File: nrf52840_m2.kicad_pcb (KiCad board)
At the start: 4 copper layers, 22 x 25.5 mm, 64 parts, among them J1 Bus_M.2_Socket_B, J2 Jlink-Tag connect, Q1 pmos, U1 nRF52840, U2 AP2112K-3.3, U3 MCP73831-2-OT, Y1 32.768kHz, Y2 32MHz

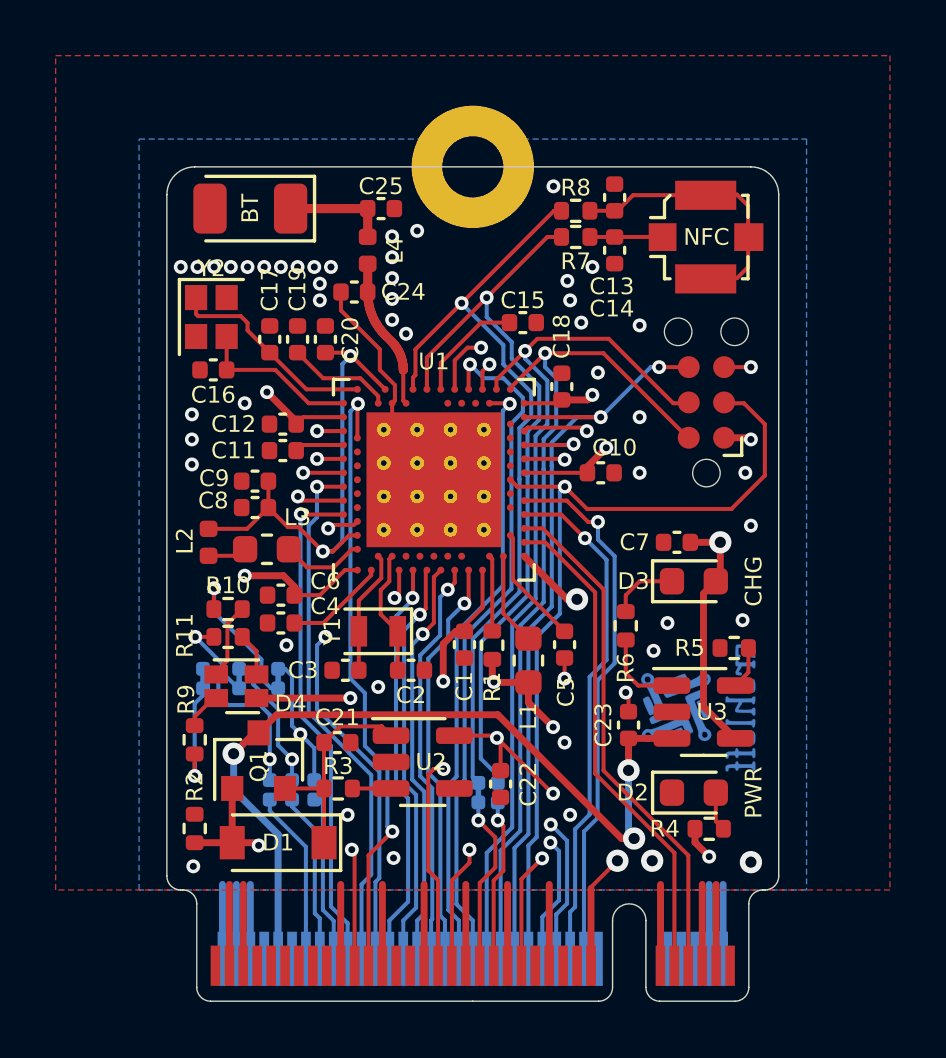
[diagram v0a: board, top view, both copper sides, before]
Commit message: update 3D/docs/fiducials
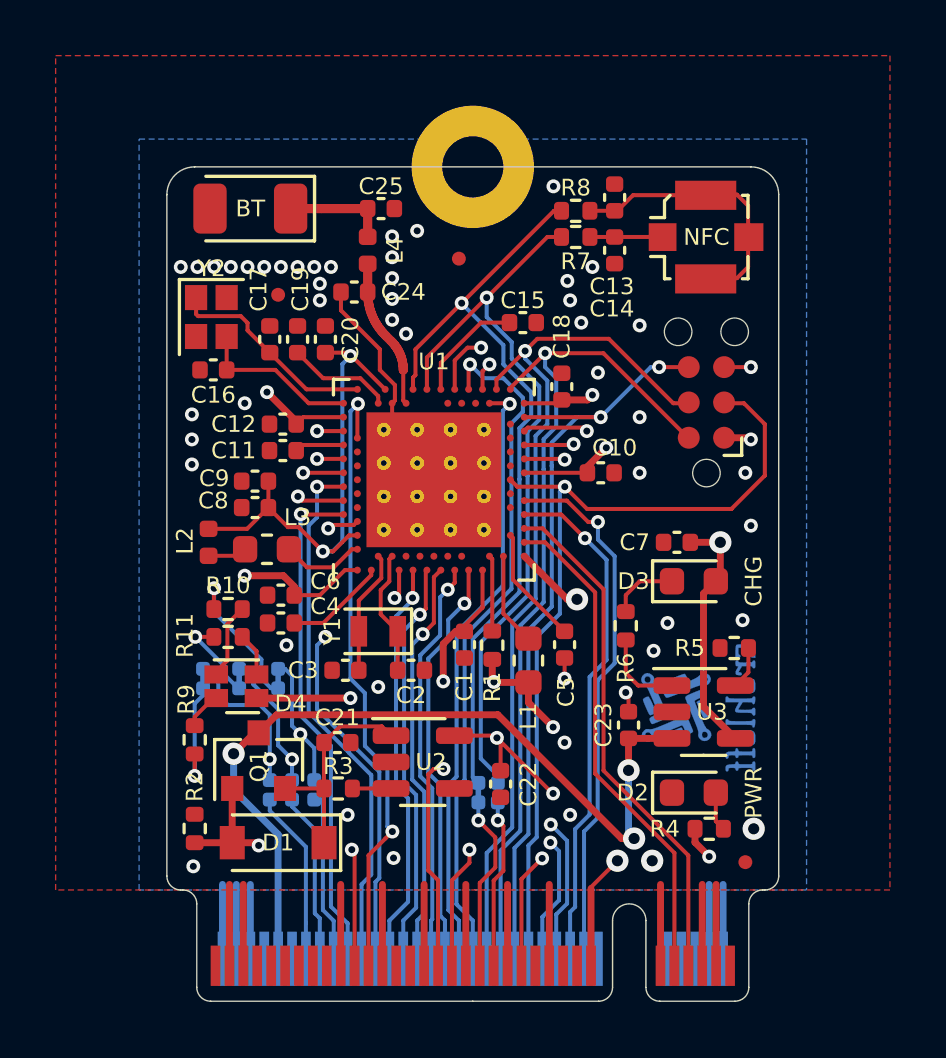
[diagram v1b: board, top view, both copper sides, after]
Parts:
- added FID1: Fiducial, Fiducial:Fiducial_0.5mm_Mask1mm, F.Cu at (228.8, 149.0)
- added FID2: Fiducial, Fiducial:Fiducial_0.5mm_Mask1mm, F.Cu at (212.0, 128.6)
- added FID3: Fiducial, Fiducial:Fiducial_0.5mm_Mask1mm, F.Cu at (218.5, 127.3)

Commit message: update files
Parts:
- moved FID1 0.51 mm to (229.2, 149.2)
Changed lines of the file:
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@@
       (effects (font (size 0.8 0.8) (thickness 0.12)))
     )
-    (pad 2 smd roundrect (at 1.45 0 180) (size 1.2 1.8) (layers F.Cu F.Paste F.Mask) (roundrect_rratio 0.208333)
+    (pad 2 smd roundrect (at 1.45 0 180) (size 1.2 1.8) (layers F.Cu F.Paste F.Mask) (roundrect_rratio 0.2083325)
       (net 23 "Net-(AE1-Pad2)"))
-    (pad 1 smd roundrect (at -1.45 0 180) (size 1.2 1.8) (layers F.Cu F.Paste F.Mask) (roundrect_rratio 0.208333)
+    (pad 1 smd roundrect (at -1.45 0 180) (size 1.2 1.8) (layers F.Cu F.Paste F.Mask) (roundrect_rratio 0.2083325)
       (net 22 "Net-(AE1-Pad1)"))
     (model ${KISYS3DMOD}/RF_Antenna.3dshapes/Johanson_2450AT18x100.wrl
@@
   )
   (module Fiducial:Fiducial_0.5mm_Mask1mm (layer F.Cu)
-    (at 228.8 149)
+    (at 229.25 149.25)
     (descr "Circular Fiducial, 0.5mm bare copper, 1mm soldermask opening (Level C)")
     (tags fiducial)
@@
       (effects (font (size 1 1) (thickness 0.15)))
     )
+    (fp_circle (center 0 0) (end 0.5 0) (layer F.Fab) (width 0.1))
+    (fp_circle (center 0 0) (end 0.75 0) (layer F.CrtYd) (width 0.05))
     (fp_text user %R (at 0 0) (layer F.Fab)
       (effects (font (size 0.2 0.2) (thickness 0.04)))
     )
-    (fp_circle (center 0 0) (end 0.5 0) (layer F.Fab) (width 0.1))
-    (fp_circle (center 0 0) (end 0.75 0) (layer F.CrtYd) (width 0.05))
     (pad "" smd circle (at 0 0) (size 0.5 0.5) (layers F.Cu F.Mask)
       (solder_mask_margin 0.25) (clearance 0.25))

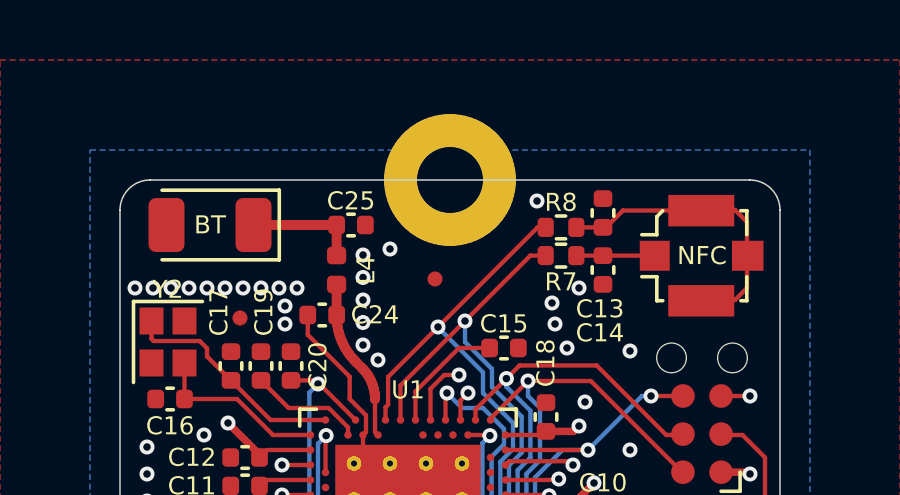
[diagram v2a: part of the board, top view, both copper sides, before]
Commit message: adjust m.2 mounting diameter
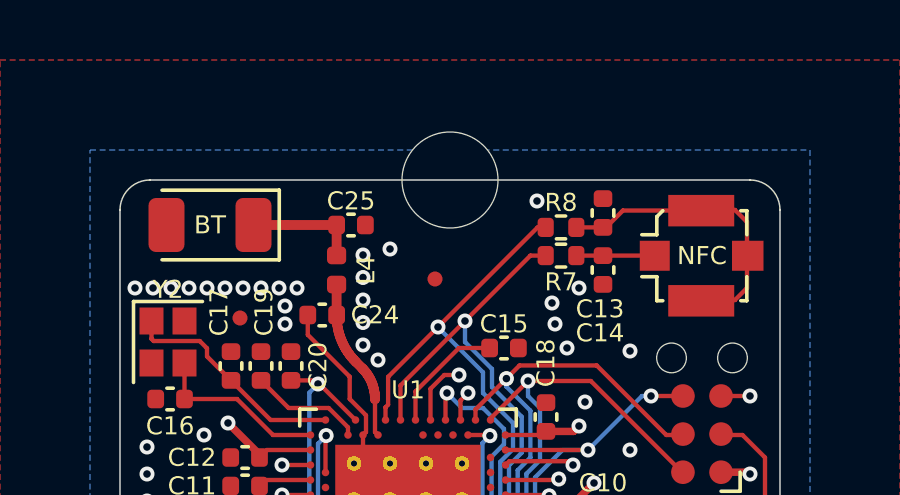
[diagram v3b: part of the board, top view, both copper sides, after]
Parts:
- H1: footprint MountingHole:MountingHole_2.2mm_M2_Pad -> MountingHole:MountingHole_3.2mm_M3
